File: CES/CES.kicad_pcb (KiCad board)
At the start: 2 copper layers, 173 parts, among them J101 Barrel_Jack, J1201 PannelPowerConnector, J1301 PanelRT, J1302 PanelMem, J1303 PanelEnd, J1401 InputDataSwitches, J1402 InputAddressSwitches, J1501 PannelButtonsConnector, J1601 ClockSelector, J1701 AddressBusConnector, J1702 DataBusConnector, J1703 RTConnector, J1704 MemSignalsConnector, U1001 74HC02, U1002 74HC30, U1003 74HC10, U1004 74HC08, U1101 SST39SF020, U1102 SST39SF020, U1103 IS61C256, U1104 IS61C256, U1301 74HC04, U1302 74HC04, U1303 74HC04, U1304 74HC04, U1305 74HC04, U1306 74HC04, U1307 74HC04, U1308 74HC04, U1401 BD1, U1402 BS1, U1403 BD2, U1404 BS2, U1405 BE1, U1406 BE2, U1501 74HC00, U1502 74HC14, U1601 74HC04, U1602 74HC4040, U201 CD1, U202 CD2, U203 CD3, U204 CD4, U205 SM1, U206 SM2, U207 SM3, U208 SM4, U209 ME1, U210 ME2, U211 ME3, U212 ME4, U401 RT1, U402 RT2, U403 RT3, U404 RT4, U405 BT1, U406 BT2, U501 RP1, U502 RP2, U503 RP3, U504 RP4, U601 RD1, U602 RD2, U603 RD3, U604 RD4, U701 RE1, U702 RE2, U703 RE3, U704 RE4, U801 74HC21, U802 74HC20, U803 74HC00, U804 74HC02, U805 74HC27, U806 74HC27, U807 74HC02, U808 74HC20, U809 74HC00, U901 RC, U902 Est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

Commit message: Correcting footprints errors
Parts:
- removed U905, U906: 74HC74, Package_DIP:DIP-14_W7.62mm
- removed U907: RI0, Package_DIP:DIP-14_W7.62mm
- removed U908: Para, Package_DIP:DIP-16_W7.62mm
- removed U909: Partiu, Package_DIP:DIP-16_W7.62mm
- added C505: C, Capacitor_THT:C_Disc_D4.3mm_W1.9mm_P5.00mm, F.Cu at (15.0, 185.2)
- added R501: R, Resistor_THT:R_Axial_DIN0204_L3.6mm_D1.6mm_P1.90mm_Vertical, F.Cu at (58.4, 163.2)
- C1001, C1002, C1003, C1004, C1101, C1102, C1103, C1104, C1301, C1302, C1303, C1304, C1305, C1306, C1307, C1308, C1401, C1402, C1403, C1404, C1405, C1406, C1501, C1601, C1602, C1603, C1604, C1605, C201, C202, C203, C204, C205, C206, C207, C208, C209, C210, C211, C212, C401, C402, C403, C404, C405, C406, C501, C502, C503, C504, C601, C602, C603, C604, C701, C702, C703, C704, C801, C802, C803, C804, C805, C806, C807, C808, C809, C901, C902, C903, C904: footprint Capacitor_THT:CP_Radial_D5.0mm_P2.50mm -> Capacitor_THT:C_Disc_D4.3mm_W1.9mm_P5.00mm
- J1301: value PanelRT -> Conn_01x16
- J1302: value PanelMem -> Conn_01x16
- J1303: value PanelEnd -> Conn_01x16
- J1601: value ClockSelector -> Conn_02x12
- J1701: value AddressBusConnector -> Conn_01x16
- J1702: value DataBusConnector -> Conn_01x16
- J1703: value RTConnector -> Conn_01x16
- J1704: value MemSignalsConnector -> Conn_01x07
- U1001: value 74HC02 -> 74HC30
- U1002: value 74HC30 -> 74HC08
- U1003: value 74HC10 -> 74HC02
- U1004: value 74HC08 -> 74HC10
- U1401: value BD1 -> 74HC244
- U1402: value BS1 -> 74HC244
- U1403: value BD2 -> 74HC244
- U1404: value BS2 -> 74HC244
- U1405: value BE1 -> 74HC244
- U1406: value BE2 -> 74HC244
- U201: value CD1 -> 74HC02
- U202: value CD2 -> 74HC02
- U203: value CD3 -> 74HC02
- U204: value CD4 -> 74HC02
- U205: value SM1 -> 74HC283
- U206: value SM2 -> 74HC283
- U207: value SM3 -> 74HC283
- U208: value SM4 -> 74HC283
- U209: value ME1 -> 74HC257
- U210: value ME2 -> 74HC257
- U211: value ME3 -> 74HC257
- U212: value ME4 -> 74HC257
- U401: value RT1 -> 74HC173
- U402: value RT2 -> 74HC173
- U403: value RT3 -> 74HC173
- U404: value RT4 -> 74HC173
- U405: value BT1 -> 74HC244
- U406: value BT2 -> 74HC244
- U501: value RP1 -> 74HC173
- U502: value RP2 -> 74HC173
- U503: value RP3 -> 74HC173
- U504: value RP4 -> 74HC173
- U601: value RD1 -> 74HC173
- U602: value RD2 -> 74HC173
- U603: value RD3 -> 74HC173
- U604: value RD4 -> 74HC173
- U701: value RE1 -> 74HC173
- U702: value RE2 -> 74HC173
- U703: value RE3 -> 74HC173
- U704: value RE4 -> 74HC173
- U801, U802, U808: footprint Package_DIP:DIP-12_W7.62mm -> Package_DIP:DIP-14_W7.62mm
- U901: value RC -> 74HC74
- U902: value Est -> 74HC175; footprint Package_DIP:DIP-14_W7.62mm -> Package_DIP:DIP-16_W7.62mm
- U903: value RS:Parte -> 74HC112
- U904: value 74HC112 -> 74HC74; footprint Package_DIP:DIP-16_W7.62mm -> Package_DIP:DIP-14_W7.62mm
- Y1601: footprint Crystal:Crystal_HC33-U_Vertical -> Crystal:Crystal_HC52-U_Vertical
- moved C503 293.0 mm to (31.3, 185.2)
- moved U504 289.9 mm to (15.1, 163.7)
- moved C1101 283.4 mm to (-119.6, 48.6)
- moved U503 269.6 mm to (25.9, 163.7)
- moved C1102 267.8 mm to (-103.3, 48.6)
- moved C1104 252.7 mm to (-111.4, 48.6)
- moved C504 252.0 mm to (23.2, 185.2)
- moved U502 249.6 mm to (36.8, 163.7)
- moved C502 249.2 mm to (39.5, 185.2)
- moved C501 235.7 mm to (47.6, 185.2)
- moved U501 229.9 mm to (47.6, 163.7)
- moved C1103 229.0 mm to (-59.1, 6.27)
- moved U1101 221.7 mm to (-99.7, 6.67)
- moved U1102 221.7 mm to (-119.1, 6.67)
- moved U1103 221.7 mm to (-69.9, 6.62)
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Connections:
- C1001 pad 2: EGND -> GND
- C1002 pad 2: EGND -> GND
- C1003 pad 2: EGND -> GND
- C1004 pad 2: EGND -> GND
- C101 pad 2: EGND -> GND
- C102 pad 2: EGND -> GND
- C103 pad 2: EGND -> GND
- C1101 pad 2: EGND -> GND
- C1102 pad 2: EGND -> GND
- C1103 pad 2: EGND -> GND
- C1104 pad 2: EGND -> GND
- C1301 pad 2: EGND -> GND
- C1302 pad 2: EGND -> GND
- C1303 pad 2: EGND -> GND
- C1304 pad 2: EGND -> GND
- C1305 pad 2: EGND -> GND
- C1306 pad 2: EGND -> GND
- C1307 pad 2: EGND -> GND
- C1308 pad 2: EGND -> GND
- C1401 pad 2: EGND -> GND
- C1402 pad 2: EGND -> GND
- C1403 pad 2: EGND -> GND
- C1404 pad 2: EGND -> GND
- C1405 pad 2: EGND -> GND
- C1406 pad 2: EGND -> GND
- C1501 pad 2: EGND -> GND
- C1601 pad 2: EGND -> GND
- C1602 pad 2: EGND -> GND
- C1603 pad 2: EGND -> GND
- C1604 pad 2: EGND -> GND
- C1605 pad 2: EGND -> GND
- C201 pad 2: EGND -> GND
- C202 pad 2: EGND -> GND
- C203 pad 2: EGND -> GND
- C204 pad 2: EGND -> GND
- C205 pad 2: EGND -> GND
- C206 pad 2: EGND -> GND
- C207 pad 2: EGND -> GND
- C208 pad 2: EGND -> GND
- C209 pad 2: EGND -> GND
- C210 pad 2: EGND -> GND
- C211 pad 2: EGND -> GND
- C212 pad 2: EGND -> GND
- C401 pad 2: EGND -> GND
- C402 pad 2: EGND -> GND
- C403 pad 2: EGND -> GND
- C404 pad 2: EGND -> GND
- C405 pad 2: EGND -> GND
- C406 pad 2: EGND -> GND
- C501 pad 2: EGND -> GND
- C502 pad 2: EGND -> GND
- C503 pad 2: EGND -> GND
- C504 pad 2: EGND -> GND
- C601 pad 2: EGND -> GND
- C602 pad 2: EGND -> GND
- C603 pad 2: EGND -> GND
- C604 pad 2: EGND -> GND
- C701 pad 2: EGND -> GND
- C702 pad 2: EGND -> GND
- C703 pad 2: EGND -> GND
- C704 pad 2: EGND -> GND
- C801 pad 2: EGND -> GND
- C802 pad 2: EGND -> GND
- C803 pad 2: EGND -> GND
- C804 pad 2: EGND -> GND
- C805 pad 2: EGND -> GND
- C806 pad 2: EGND -> GND
- C807 pad 2: EGND -> GND
- C808 pad 2: EGND -> GND
- C809 pad 2: EGND -> GND
- C901 pad 2: EGND -> GND
- C902 pad 2: EGND -> GND
- C903 pad 2: EGND -> GND
- C904 pad 2: EGND -> GND
- J101 pad 2: EGND -> GND
- J1201 pad 1: EGND -> GND
- J1201 pad 2: EGND -> GND
- J1402 pad 15: Net-(J1402-Pad15) -> (no net)
- J1402 pad 16: Net-(J1402-Pad16) -> (no net)
- J1701 pad 15: Net-(J1701-Pad15) -> (no net)
- J1701 pad 16: Net-(J1701-Pad16) -> (no net)
- J1704 pad 3: EGND -> GND
- J1704 pad 4: EGND -> GND
- U1001 pad 1: Net-(U1001-Pad1) -> A13
- U1001 pad 10: ~HabSelRAM -> (no net)
- U1001 pad 11: A13 -> A7
- U1001 pad 12: A12 -> A6
- U1001 pad 13: Net-(U1001-Pad13) -> (no net)
- U1001 pad 2: A10 -> A12
- U1001 pad 4: Net-(U1001-Pad4) -> A10
- U1001 pad 5: EGND -> A9
- U1001 pad 6: EGND -> A8
- U1001 pad 7: EGND -> GND
- U1001 pad 9: Net-(U1001-Pad9) -> (no net)
- U1002 pad 1: A13 -> Net-(U1002-Pad1)
- U1002 pad 10: (no net) -> GND
- U1002 pad 11: A7 -> (no net)
- U1002 pad 12: A6 -> GND
- U1002 pad 13: (no net) -> GND
- U1002 pad 2: A12 -> Net-(U1002-Pad2)
- U1002 pad 3: A11 -> ~SelRam
- U1002 pad 4: A10 -> GND
- U1002 pad 5: A9 -> GND
- U1002 pad 6: A8 -> (no net)
- U1002 pad 7: EGND -> GND
- U1002 pad 8: Net-(U1001-Pad8) -> (no net)
- U1002 pad 9: (no net) -> GND
- U1003 pad 1: Net-(U1001-Pad1) -> Net-(U1002-Pad1)
- U1003 pad 10: EGND -> ~HabSelRAM
- U1003 pad 11: EGND -> A13
- U1003 pad 12: ~LeRom -> A12
- U1003 pad 13: ~EscMem -> Net-(U1002-Pad2)
- U1003 pad 2: Net-(U1001-Pad13) -> A10
- U1003 pad 3: A5 -> A11
- U1003 pad 4: A4 -> (no net)
- U1003 pad 5: VCC -> GND
- U1003 pad 6: Net-(U1001-Pad9) -> GND
- U1003 pad 7: EGND -> GND
- U1003 pad 8: Net-(U1003-Pad8) -> Net-(U1001-Pad8)
- U1003 pad 9: EGND -> Net-(U1003-Pad9)
- U1004 pad 1: Net-(U1001-Pad1) -> Net-(U1002-Pad1)
- U1004 pad 10: EGND -> GND
- U1004 pad 11: Net-(U1004-Pad11) -> GND
- U1004 pad 12: EGND -> ~LeRom
- U1004 pad 13: EGND -> ~EscMem
- U1004 pad 2: Net-(U1001-Pad13) -> Net-(U1002-Pad2)
- U1004 pad 3: ~SelRam -> A5
- U1004 pad 4: EGND -> A4
- U1004 pad 5: EGND -> VCC
- U1004 pad 6: Net-(U1004-Pad6) -> Net-(U1003-Pad9)
- U1004 pad 7: EGND -> GND
- U1004 pad 8: Net-(U1004-Pad8) -> (no net)
- U1004 pad 9: EGND -> GND
- U1101 pad 1: EGND -> GND
- U1101 pad 16: EGND -> GND
- U1101 pad 2: EGND -> GND
- U1101 pad 22: EGND -> GND
- U1101 pad 23: EGND -> GND
- U1101 pad 25: EGND -> GND
- U1101 pad 28: EGND -> GND
- U1101 pad 29: EGND -> GND
- U1101 pad 3: EGND -> GND
- U1101 pad 30: EGND -> GND
- U1101 pad 4: EGND -> GND
- U1102 pad 1: EGND -> GND
- U1102 pad 16: EGND -> GND
- U1102 pad 2: EGND -> GND
- U1102 pad 22: EGND -> GND
- U1102 pad 23: EGND -> GND
- U1102 pad 25: EGND -> GND
- U1102 pad 28: EGND -> GND
- U1102 pad 29: EGND -> GND
- U1102 pad 3: EGND -> GND
- U1102 pad 30: EGND -> GND
- U1102 pad 4: EGND -> GND
- U1103 pad 1: EGND -> GND
- U1103 pad 14: EGND -> GND
- U1103 pad 21: (no net) -> A10
- U1104 pad 1: EGND -> GND
- U1104 pad 14: EGND -> GND
- U1104 pad 21: (no net) -> A10
- U1301 pad 7: EGND -> GND
- U1302 pad 7: EGND -> GND
- U1303 pad 7: EGND -> GND
- U1304 pad 7: EGND -> GND
- U1305 pad 7: EGND -> GND
- U1306 pad 7: EGND -> GND
- U1307 pad 7: EGND -> GND
- U1308 pad 7: EGND -> GND
- U1401 pad 10: EGND -> GND
- U1402 pad 10: EGND -> GND
- U1403 pad 10: EGND -> GND
- U1404 pad 10: EGND -> GND
- U1405 pad 10: EGND -> GND
- U1406 pad 10: EGND -> GND
- U1406 pad 11: EGND -> GND
- U1406 pad 13: EGND -> GND
- U1406 pad 7: Net-(U1406-Pad7) -> (no net)
- U1406 pad 9: Net-(U1406-Pad9) -> (no net)
- U1501 pad 10: EGND -> GND
- U1501 pad 11: Net-(U1501-Pad11) -> (no net)
- U1501 pad 12: EGND -> GND
- U1501 pad 13: EGND -> GND
- U1501 pad 7: EGND -> GND
- U1501 pad 8: Net-(U1501-Pad8) -> (no net)
- U1501 pad 9: EGND -> GND
- U1502 pad 7: EGND -> GND
- U1601 pad 10: Net-(U1601-Pad10) -> (no net)
- U1601 pad 11: EGND -> GND
- U1601 pad 12: Net-(U1601-Pad12) -> (no net)
- U1601 pad 13: EGND -> GND
- U1601 pad 5: EGND -> GND
- U1601 pad 6: Net-(U1601-Pad6) -> (no net)
- U1601 pad 7: EGND -> GND
- U1601 pad 8: Net-(U1601-Pad8) -> (no net)
- U1601 pad 9: EGND -> GND
- U1602 pad 11: EGND -> GND
- U1602 pad 8: EGND -> GND
- U201 pad 7: EGND -> GND
- U202 pad 7: EGND -> GND
- U203 pad 7: EGND -> GND
- U204 pad 7: EGND -> GND
- U205 pad 8: EGND -> GND
- U206 pad 8: EGND -> GND
- U207 pad 8: EGND -> GND
- U208 pad 8: EGND -> GND
- U209 pad 15: EGND -> GND
- U209 pad 8: EGND -> GND
- U210 pad 15: EGND -> GND
- U210 pad 8: EGND -> GND
- U211 pad 15: EGND -> GND
- U211 pad 8: EGND -> GND
- U212 pad 10: EGND -> GND
- U212 pad 11: EGND -> GND
- U212 pad 12: Net-(U212-Pad12) -> (no net)
- U212 pad 13: EGND -> GND
- U212 pad 14: EGND -> GND
- U212 pad 15: EGND -> GND
- U212 pad 8: EGND -> GND
- U212 pad 9: Net-(U212-Pad9) -> (no net)
- U401 pad 1: EGND -> GND
- U401 pad 10: EGND -> GND
- U401 pad 15: EGND -> GND
- U401 pad 2: EGND -> GND
- U401 pad 8: EGND -> GND
- U402 pad 1: EGND -> GND
- U402 pad 10: EGND -> GND
- U402 pad 15: EGND -> GND
- U402 pad 2: EGND -> GND
- U402 pad 8: EGND -> GND
- U403 pad 1: EGND -> GND
- U403 pad 10: EGND -> GND
- U403 pad 15: EGND -> GND
- U403 pad 2: EGND -> GND
- U403 pad 8: EGND -> GND
- U404 pad 1: EGND -> GND
- U404 pad 10: EGND -> GND
- U404 pad 15: EGND -> GND
- U404 pad 2: EGND -> GND
- U404 pad 8: EGND -> GND
- U405 pad 10: EGND -> GND
- U406 pad 10: EGND -> GND
- U501 pad 10: EGND -> GND
- U501 pad 15: EGND -> Net-(C505-Pad2)
- U501 pad 2: EGND -> GND
- U501 pad 8: EGND -> GND
- U502 pad 10: EGND -> GND
- U502 pad 15: EGND -> Net-(C505-Pad2)
- U502 pad 2: EGND -> GND
- U502 pad 8: EGND -> GND
- U503 pad 10: EGND -> GND
- U503 pad 15: EGND -> Net-(C505-Pad2)
- U503 pad 2: EGND -> GND
- U503 pad 8: EGND -> GND
- U504 pad 10: EGND -> GND
- U504 pad 15: EGND -> Net-(C505-Pad2)
- U504 pad 2: EGND -> GND
- U504 pad 8: EGND -> GND
- U601 pad 10: EGND -> GND
- U601 pad 15: EGND -> GND
- U601 pad 2: EGND -> GND
- U601 pad 8: EGND -> GND
- U601 pad 9: EGND -> GND
- U602 pad 10: EGND -> GND
- U602 pad 15: EGND -> GND
- U602 pad 2: EGND -> GND
- U602 pad 8: EGND -> GND
- U602 pad 9: EGND -> GND
- U603 pad 10: EGND -> GND
- U603 pad 15: EGND -> GND
- U603 pad 2: EGND -> GND
- U603 pad 8: EGND -> GND
- U603 pad 9: EGND -> GND
- U604 pad 10: EGND -> GND
- U604 pad 15: EGND -> GND
- U604 pad 2: EGND -> GND
- U604 pad 8: EGND -> GND
- U604 pad 9: EGND -> GND
- U701 pad 10: EGND -> GND
- U701 pad 15: EGND -> GND
- U701 pad 2: EGND -> GND
- U701 pad 8: EGND -> GND
- U701 pad 9: EGND -> GND
- U702 pad 10: EGND -> GND
- U702 pad 15: EGND -> GND
- U702 pad 2: EGND -> GND
- U702 pad 8: EGND -> GND
- U702 pad 9: EGND -> GND
- U703 pad 10: EGND -> GND
- U703 pad 15: EGND -> GND
- U703 pad 2: EGND -> GND
- U703 pad 8: EGND -> GND
- U703 pad 9: EGND -> GND
- U704 pad 10: EGND -> GND
- U704 pad 11: EGND -> GND
- U704 pad 12: EGND -> GND
- U704 pad 15: EGND -> GND
- U704 pad 2: EGND -> GND
- U704 pad 5: Net-(U704-Pad5) -> (no net)
- U704 pad 6: Net-(U704-Pad6) -> (no net)
- U704 pad 8: EGND -> GND
- U704 pad 9: EGND -> GND
- U801 pad 7: EGND -> GND
- U802 pad 7: EGND -> GND
- U803 pad 7: EGND -> GND
- U804 pad 12: EGND -> GND
- U804 pad 3: EGND -> GND
- U804 pad 7: EGND -> GND
- U805 pad 11: EGND -> GND
- U805 pad 7: EGND -> GND
- U806 pad 7: EGND -> GND
- U807 pad 12: EGND -> GND
- U807 pad 7: EGND -> GND
- U808 pad 7: EGND -> GND
- U809 pad 7: EGND -> GND
- U901 pad 10: (no net) -> VCC
- U901 pad 11: (no net) -> Rlg3
- U901 pad 12: (no net) -> ~UltC
- U901 pad 13: (no net) -> VCC
- U901 pad 14: (no net) -> VCC
- U901 pad 7: (no net) -> GND
- U901 pad 8: (no net) -> ~Est1
- U901 pad 9: (no net) -> Est1
- U902 pad 1: (no net) -> VCC
- U902 pad 10: VCC -> ~BotEscMem
- U902 pad 11: Rlg3 -> BotEscMem
- U902 pad 12: ~UltC -> BotMem
- U902 pad 13: VCC -> VaiPartir
- U902 pad 14: (no net) -> ~Parte
- U902 pad 3: (no net) -> MudaT
- U902 pad 4: (no net) -> BotMudaT
- U902 pad 5: (no net) -> BotMudaP
- U902 pad 6: (no net) -> MudaP
- U902 pad 8: ~Est1 -> GND
- U902 pad 9: Est1 -> Rlg3
- U903 pad 1: VCC -> ~Rlg
- U903 pad 10: ~BotEscMem -> VCC
- U903 pad 11: BotEscMem -> Parte
- U903 pad 12: BotMem -> ~BotParteAtivo
- U903 pad 13: VaiPartir -> ~Rlg
- U903 pad 14: ~Parte -> VCC
- U903 pad 15: Parte -> VCC
- U903 pad 2: Net-(U903-Pad2) -> Parte
- U903 pad 3: MudaT -> VaiParar
- U903 pad 4: BotMudaT -> VCC
- U903 pad 5: BotMudaP -> Para
- U903 pad 6: MudaP -> ~Para
- U903 pad 7: Net-(U903-Pad7) -> ~Partiu
- U903 pad 8: EGND -> GND
- U903 pad 9: Rlg3 -> (no net)
- U904 pad 1: (no net) -> VCC
- U904 pad 10: (no net) -> VCC
- U904 pad 11: (no net) -> RlgRI
- U904 pad 12: (no net) -> VDB15
- U904 pad 13: (no net) -> VCC
- U904 pad 14: (no net) -> VCC
- U904 pad 2: (no net) -> VDB14
- U904 pad 3: (no net) -> RlgRI
- U904 pad 4: (no net) -> VCC
- U904 pad 5: (no net) -> I0
- U904 pad 6: (no net) -> ~I0
- U904 pad 7: (no net) -> GND
- U904 pad 8: EGND -> ~I1
- U904 pad 9: (no net) -> I1

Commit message: Starting PCB design
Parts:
- moved C701 432.2 mm to (-97.6, 235.2)
- moved C702 432.2 mm to (-105.7, 235.2)
- moved C704 432.2 mm to (-113.9, 235.2)
- moved C703 432.2 mm to (-122.0, 235.2)
- moved C801 407.7 mm to (-93.5, 252.1)
- moved C802 407.7 mm to (-85.3, 255.5)
- moved C803 407.7 mm to (-85.3, 252.1)
- moved C804 407.7 mm to (-93.5, 259.0)
- moved C805 407.7 mm to (-85.3, 259.0)
- moved C806 407.7 mm to (-93.5, 262.4)
- moved C807 407.7 mm to (-93.5, 265.9)
- moved C809 407.7 mm to (-93.5, 255.5)
- moved C1401 353.4 mm to (457.0, 31.4)
- moved C1402 353.4 mm to (473.3, 31.4)
- moved C1405 353.4 mm to (465.1, 31.4)
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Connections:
- U201 pad 2: SRT0 -> SRT1
- U201 pad 5: SRT1 -> SRT0
- U202 pad 2: SRT4 -> SRT5
- U202 pad 5: SRT5 -> SRT4
- U203 pad 2: SRT8 -> SRT9
- U203 pad 5: SRT9 -> SRT8
- U204 pad 2: SRT12 -> SRT13
- U204 pad 5: SRT13 -> SRT12
- U205 pad 2: Net-(U201-Pad4) -> Net-(U201-Pad1)
- U205 pad 6: Net-(U201-Pad1) -> Net-(U201-Pad4)
- U206 pad 2: Net-(U202-Pad4) -> Net-(U202-Pad1)
- U206 pad 6: Net-(U202-Pad1) -> Net-(U202-Pad4)
- U207 pad 2: Net-(U203-Pad4) -> Net-(U203-Pad1)
- U207 pad 6: Net-(U203-Pad1) -> Net-(U203-Pad4)
- U208 pad 2: Net-(U204-Pad4) -> Net-(U204-Pad1)
- U208 pad 6: Net-(U204-Pad1) -> Net-(U204-Pad4)
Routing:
- net VDB1: track 0.00 -> 100.7 mm, vias 0 -> 2
- net VDB0: track 0.00 -> 96.6 mm, vias 0 -> 1
- net VDB3: track 0.00 -> 90.1 mm, vias 0 -> 2
- net VDB2: track 0.00 -> 88.3 mm, vias 0 -> 2
- net SS1: track 0.00 -> 79.6 mm, vias 0 -> 3
- net ESA0: track 0.00 -> 67.7 mm, vias 0 -> 2
- net ESA1: track 0.00 -> 65.2 mm
- net SS0: track 0.00 -> 64.9 mm, vias 0 -> 1
- net SS3: track 0.00 -> 64.9 mm, vias 0 -> 1
- net SS2: track 0.00 -> 64.6 mm, vias 0 -> 1
- net ESA3: track 0.00 -> 63.5 mm, vias 0 -> 1
- net SRT1: track 0.00 -> 63.5 mm
- net SRT3: track 0.00 -> 61.5 mm
- net ESA2: track 0.00 -> 58.6 mm, vias 0 -> 1
- net SRT0: track 0.00 -> 55.2 mm
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
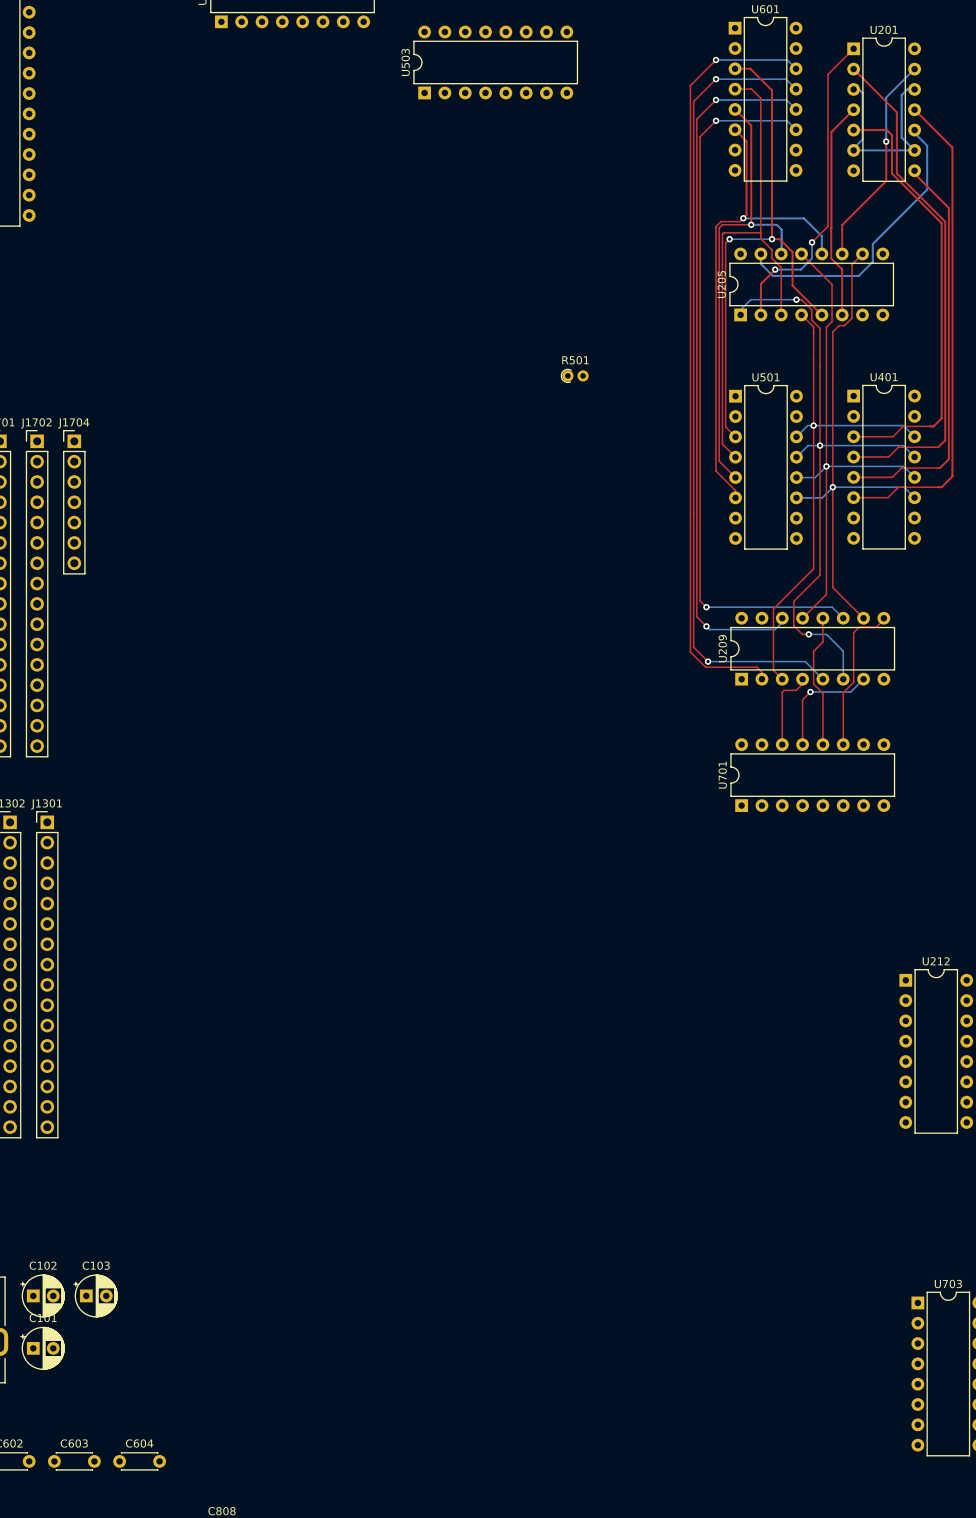
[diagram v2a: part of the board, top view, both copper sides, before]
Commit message: Simplifying tracks
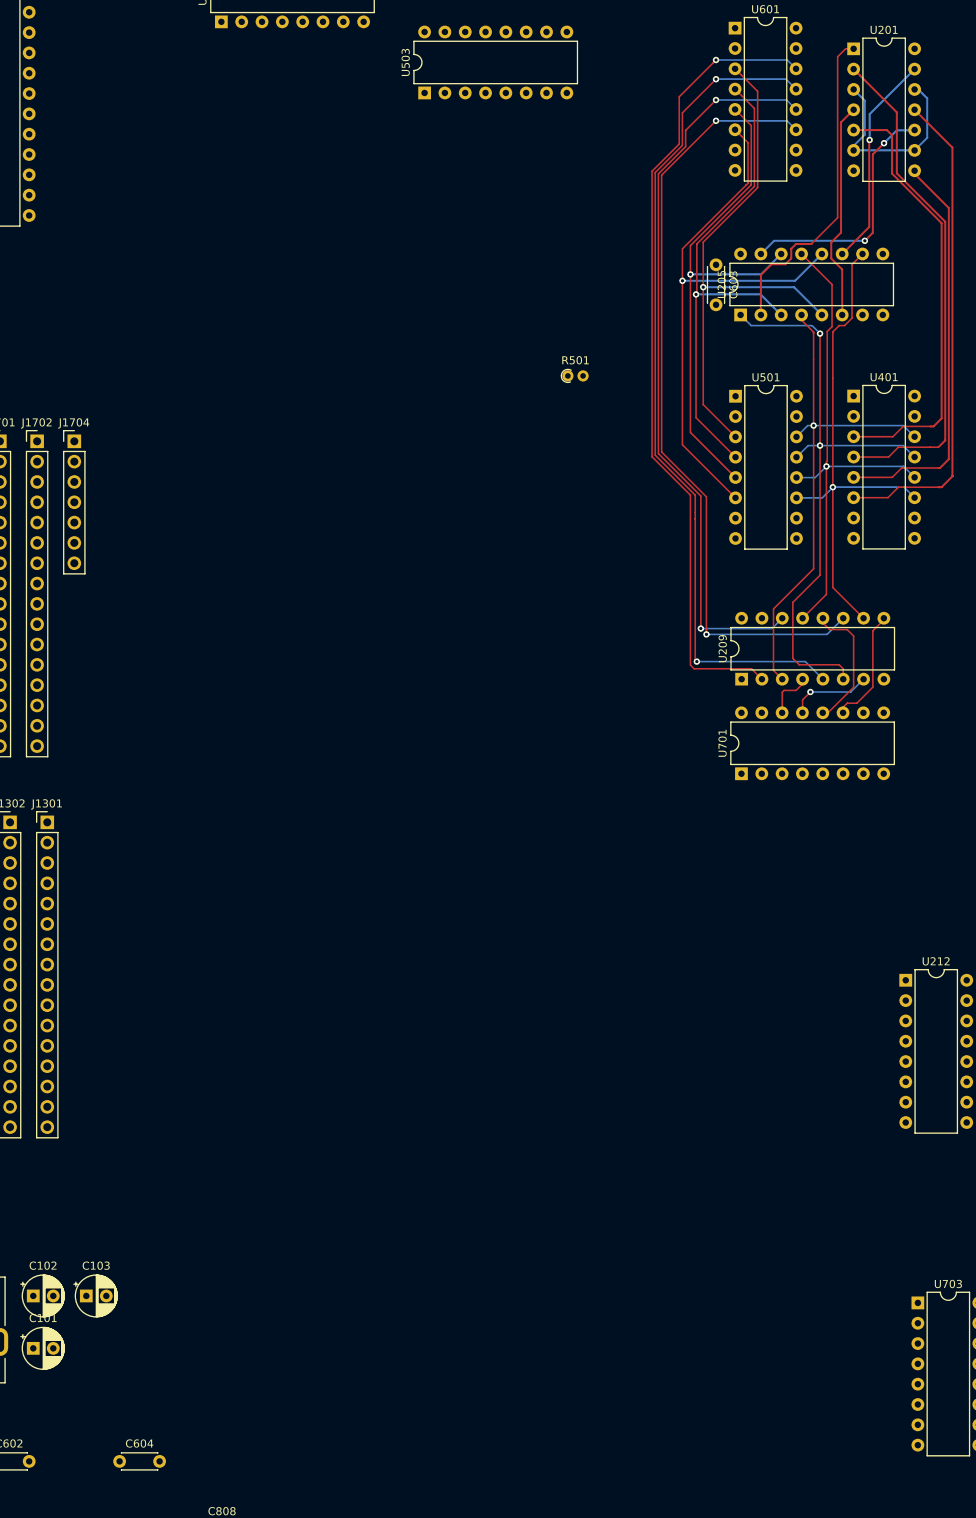
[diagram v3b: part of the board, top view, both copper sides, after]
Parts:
- moved C603 170.9 mm to (23.6, 45.8), turned to 270 degrees
- moved U701 3.98 mm to (26.8, 109.4)
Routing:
- net ESA3: track 63.5 -> 71.7 mm
- net VDB3: track 90.1 -> 97.7 mm
- net ESA2: track 58.6 -> 64.7 mm
- net Net-(U201-Pad10): track 37.1 -> 31.4 mm, vias 0 -> 2
- net VDB1: track 100.7 -> 105.4 mm
- net SME3: track 19.2 -> 14.6 mm
- net VDB0: track 96.6 -> 101.1 mm
- net VDB2: track 88.3 -> 92.4 mm
- net SME0: track 10.1 -> 6.14 mm
- net SME1: track 14.3 -> 10.3 mm
- net SS1: track 79.6 -> 77.8 mm, vias 3 -> 2
- net ESA1: track 65.2 -> 63.8 mm, vias 0 -> 1
- net Net-(U201-Pad1): track 39.9 -> 40.8 mm, vias 2 -> 0
- net ESA0: track 67.7 -> 67.9 mm, vias 2 -> 1

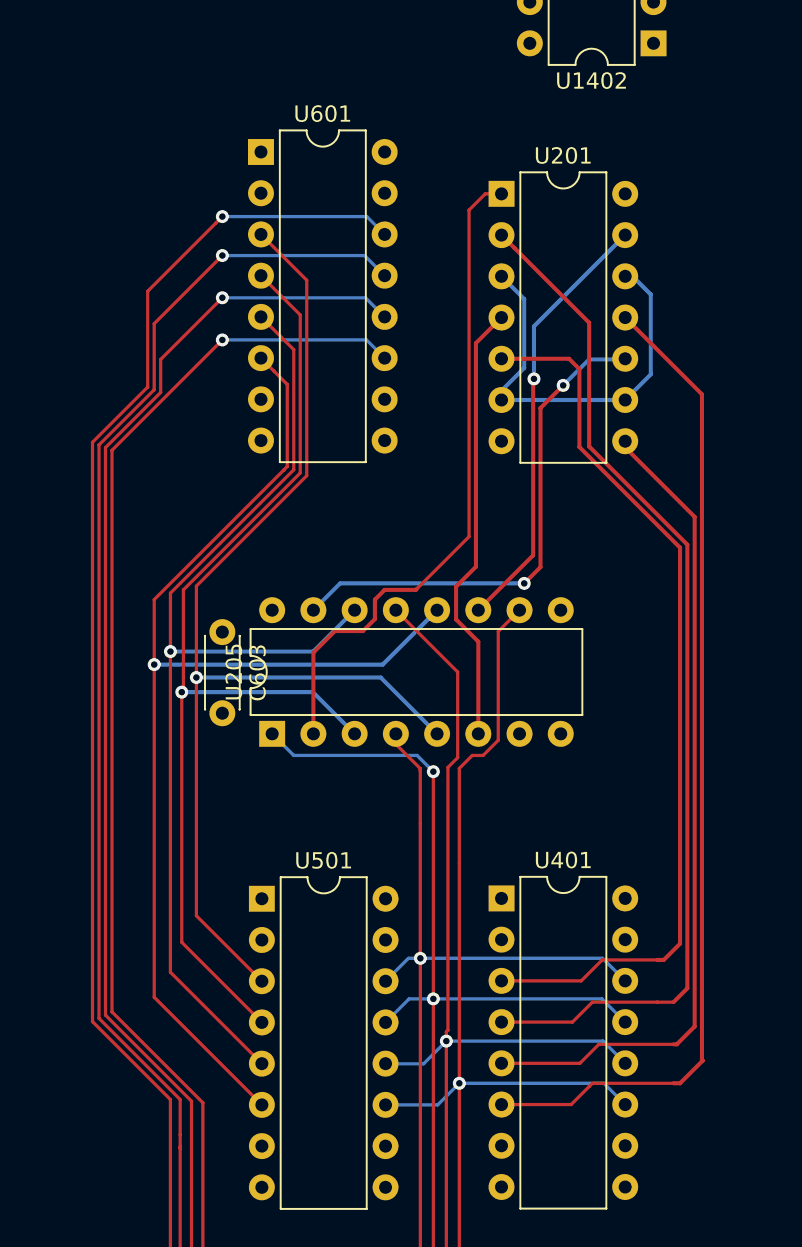
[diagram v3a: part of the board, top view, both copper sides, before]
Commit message: Minimizing used space
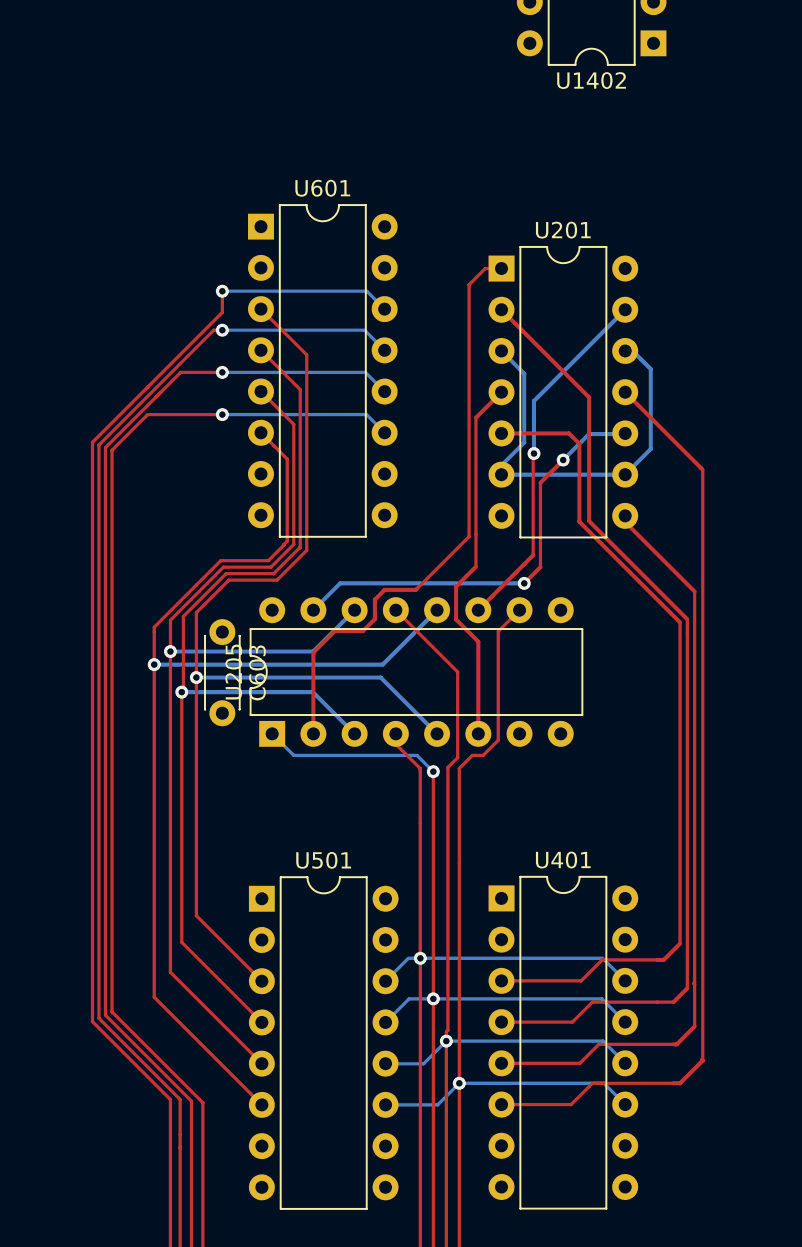
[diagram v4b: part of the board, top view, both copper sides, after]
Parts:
- moved U601 4.60 mm to (26.0, 20.8)
- moved U201 4.60 mm to (40.8, 23.4)
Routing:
- net VDB0: track 101.1 -> 96.5 mm
- net Net-(U201-Pad13): track 26.9 -> 22.3 mm
- net SRT1: track 63.5 -> 58.9 mm
- net Net-(U201-Pad10): track 31.4 -> 26.8 mm
- net Net-(U201-Pad1): track 40.8 -> 36.2 mm
- net Net-(U201-Pad4): track 27.4 -> 22.8 mm
- net SRT0: track 55.2 -> 50.6 mm
- net SRT2: track 50.7 -> 46.1 mm
- net SRT3: track 61.5 -> 57.0 mm
- net VDB1: track 105.4 -> 101.1 mm
- net ESA2: track 64.7 -> 61.8 mm
- net ESA3: track 71.7 -> 68.8 mm
- net ESA0: track 67.9 -> 65.1 mm
- net ESA1: track 63.8 -> 60.9 mm
- net VDB2: track 92.4 -> 89.8 mm
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
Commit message: Wiring BT
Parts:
- moved C204 577.3 mm to (-27.2, 237.2)
- moved C210 577.3 mm to (-35.3, 237.2)
- moved C212 577.3 mm to (-43.5, 237.2)
- moved U405 93.7 mm to (58.6, 46.9)
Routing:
- net VDB0: track 96.5 -> 153.7 mm, vias 1 -> 2
- net VDB2: track 89.8 -> 144.2 mm, vias 2 -> 3
- net VDB3: track 95.8 -> 149.9 mm, vias 2 -> 3
- net VDB1: track 101.1 -> 153.3 mm, vias 2 -> 3
- net SRT0: track 50.6 -> 57.5 mm, vias 0 -> 1
- net SRT1: track 58.9 -> 65.3 mm, vias 0 -> 1
- net SRT2: track 46.1 -> 52.0 mm, vias 0 -> 1
- net SRT3: track 57.0 -> 62.3 mm, vias 0 -> 1
- net SS1: track 77.8 -> 78.8 mm

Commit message: Crtl+C Crlt+V
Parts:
- moved R1601 263.6 mm to (665.8, 164.0)
- moved U1403 263.6 mm to (753.2, 4.51)
- moved U1601 263.6 mm to (668.6, 141.6)
- moved C1401 263.6 mm to (720.6, 31.2)
- moved C1405 263.6 mm to (728.7, 31.2)
- moved C1501 263.6 mm to (511.1, 80.7)
- moved C1602 263.6 mm to (679.4, 146.5)
- moved J1201 263.6 mm to (482.4, 102.0)
- moved J1501 263.6 mm to (507.2, 61.9)
- moved J1601 263.6 mm to (651.2, 141.9)
- moved R1501 263.6 mm to (519.2, 80.6)
- moved R1502 263.6 mm to (537.7, 61.2)
- moved R1504 263.6 mm to (537.7, 64.3)
- moved R1602 263.6 mm to (679.4, 149.8)
- moved U1001 263.6 mm to (415.1, 253.3)
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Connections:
- U206 pad 12: ESA3 -> ESA7
- U206 pad 14: ESA2 -> ESA6
- U206 pad 3: ESA1 -> ESA5
- U206 pad 5: ESA0 -> ESA4
- U207 pad 12: ESA3 -> ESA11
- U207 pad 14: ESA2 -> ESA10
- U207 pad 3: ESA1 -> ESA9
- U207 pad 5: ESA0 -> ESA8
- U208 pad 12: ESA3 -> ESA15
- U208 pad 14: ESA2 -> ESA14
- U208 pad 3: ESA1 -> ESA13
- U208 pad 5: ESA0 -> ESA12
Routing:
- net (no net): track 0.00 -> 1549.6 mm, vias 0 -> 28
- net VDB5: track 0.00 -> 137.6 mm, vias 0 -> 3
- net VDB4: track 0.00 -> 133.6 mm, vias 0 -> 2
- net VDB7: track 0.00 -> 127.5 mm, vias 0 -> 3
- net VDB6: track 0.00 -> 125.1 mm, vias 0 -> 3
- net SRT5: track 0.00 -> 105.8 mm
- net SS5: track 0.00 -> 78.8 mm, vias 0 -> 2
- net ESA7: track 0.00 -> 68.8 mm, vias 0 -> 1
- net ESA4: track 0.00 -> 65.1 mm, vias 0 -> 1
- net SS4: track 0.00 -> 64.9 mm, vias 0 -> 1
- net SS7: track 0.00 -> 64.9 mm, vias 0 -> 1
- net SS6: track 0.00 -> 64.5 mm, vias 0 -> 1
- net ESA6: track 0.00 -> 61.8 mm, vias 0 -> 1
- net ESA5: track 0.00 -> 60.9 mm, vias 0 -> 1
- net SRT7: track 0.00 -> 57.9 mm
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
